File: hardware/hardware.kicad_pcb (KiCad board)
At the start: 2 copper layers, 25.7 x 34.4 mm, 13 parts, among them P1 CONN_01X08, P2 CONN_01X08, P3 CONN_01X02, P4 CONN_01X03

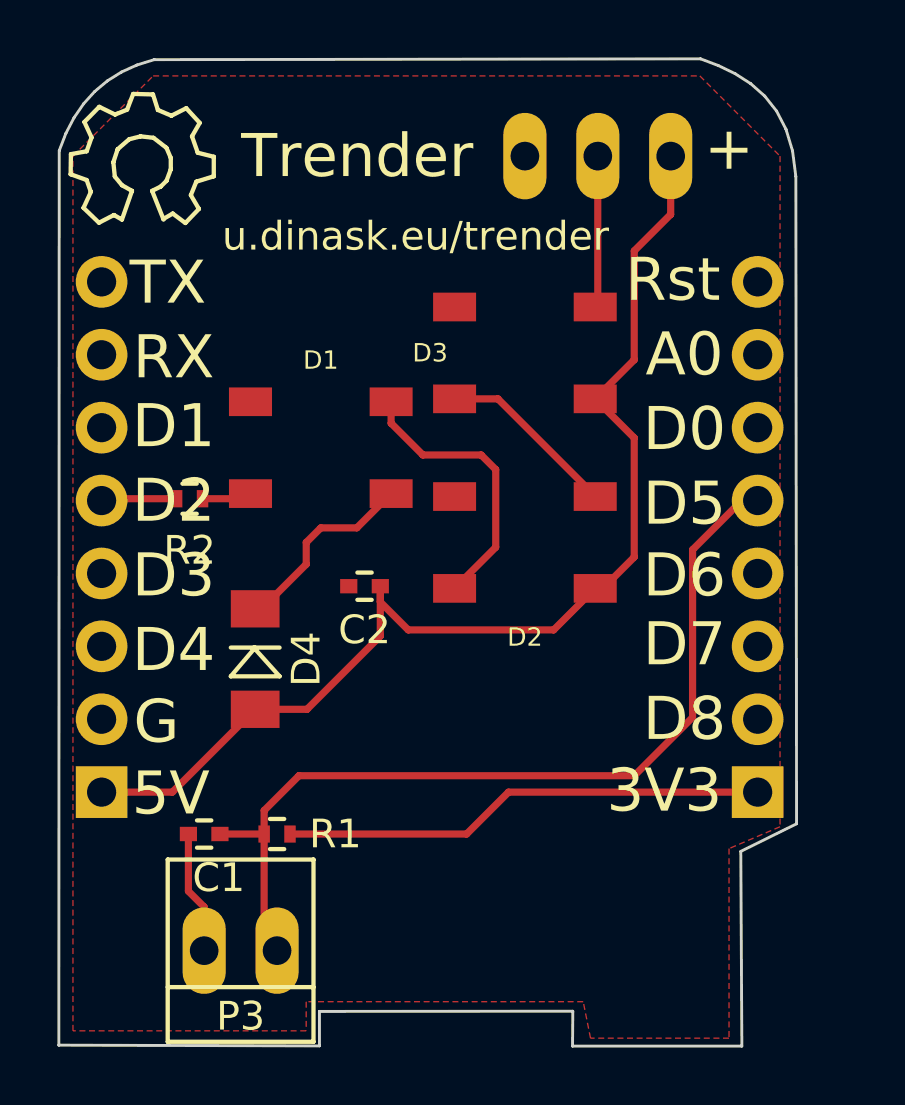
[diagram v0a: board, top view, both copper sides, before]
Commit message: v3.1, refactoring for only one Neopixel
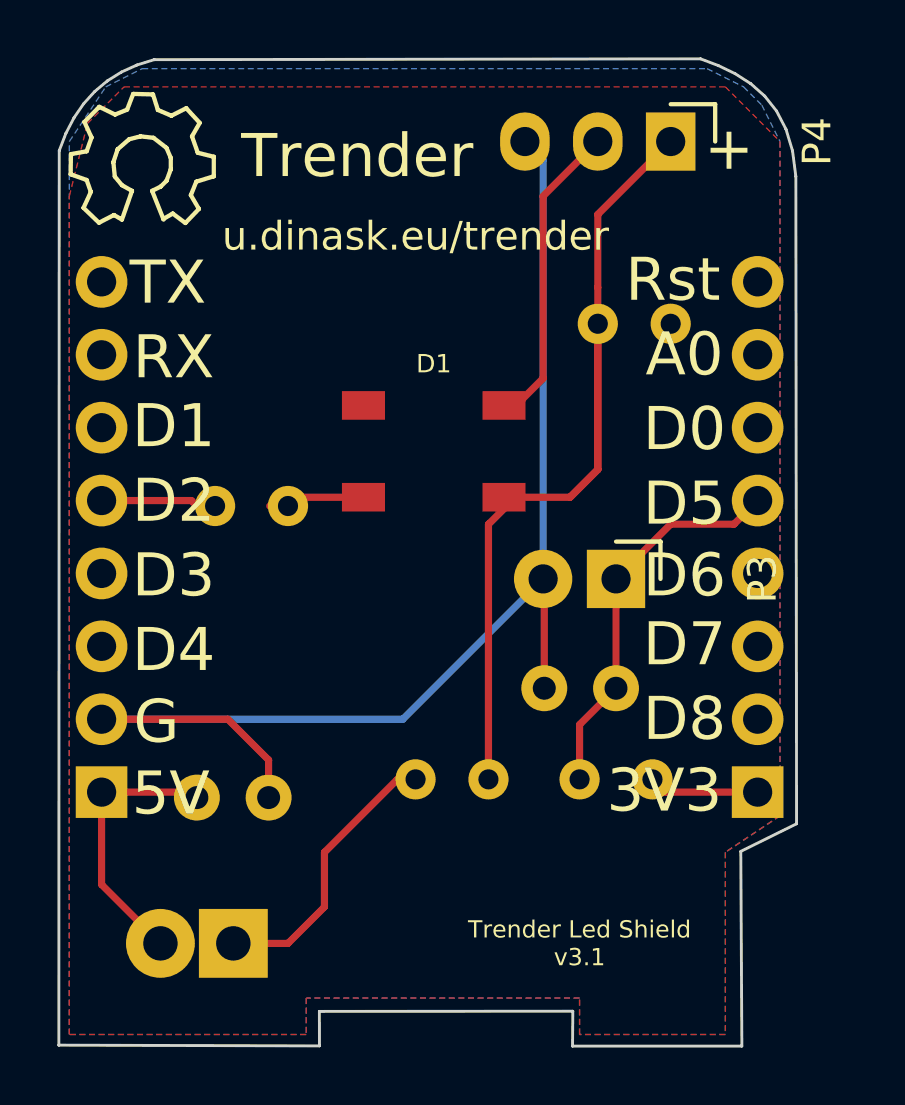
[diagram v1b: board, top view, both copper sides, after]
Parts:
- removed D2, D3: WS2812B, WS2812B:LED_WS2812B
- added R3: R, Resistors_THT:R_Axial_DIN0204_L3.6mm_D1.6mm_P2.54mm_Vertical, B.Cu at (138.4, 103.5)
- added R4: R, Resistors_THT:R_Axial_DIN0204_L3.6mm_D1.6mm_P2.54mm_Vertical, B.Cu at (144.8, 87.6)
- C1, C2: footprint Capacitors_SMD:C_0402 -> Capacitors_THT:C_Disc_D3.8mm_W2.6mm_P2.50mm; moved to B.Cu
- D4: footprint Diodes_SMD:MiniMELF_Standard -> Diodes_THT:D_DO-15_P2.54mm_Vertical_KathodeUp; moved to B.Cu
- P3: footprint Connect:PINHEAD1-2 -> Pin_Headers:Pin_Header_Angled_1x02
- P4: footprint Connect:PINHEAD1-3 -> Pin_Headers:Pin_Header_Angled_1x03; moved to F.Cu
- R1, R2: footprint Resistors_SMD:R_0402 -> Resistors_THT:R_Axial_DIN0204_L3.6mm_D1.6mm_P2.54mm_Vertical; moved to B.Cu
- moved P3 18.4 mm to (145.4, 96.5), turned to 270 degrees
- moved C1 15.2 mm to (145.4, 100.3)
- moved R1 13.2 mm to (146.7, 103.5)
- moved D4 9.94 mm to (132.1, 109.2), turned to 180 degrees
- moved C2 9.40 mm to (130.8, 104.1), turned to 0 degrees
- moved D1 3.94 mm to (139.1, 92.1)
- moved R2 3.44 mm to (134.0, 94.0)
- moved P4 2.59 mm to (147.3, 81.3), turned to 270 degrees
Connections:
- D4 pad 1: Net-(D1-Pad1) -> Net-(D4-Pad1)
- P4 pad 1: /+5V -> Net-(D1-Pad1)
- P4 pad 2: Net-(D3-Pad2) -> Net-(D1-Pad2)
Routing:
- net GND: track 4.75 -> 44.9 mm
- net /+5V: track 41.0 -> 9.52 mm
- net Net-(D1-Pad1): track 6.85 -> 32.6 mm
- net /D5: track 31.7 -> 13.8 mm
- net /+3.3V: track 16.9 -> 5.11 mm
- net Net-(D4-Pad1): track 0.00 -> 10.5 mm
- net Net-(D2-Pad2): track 6.32 -> 0.00 mm
- net Net-(D3-Pad2): track 5.30 -> 0.00 mm
- net Net-(D1-Pad4): track 2.09 -> 3.39 mm
- net Net-(D1-Pad2): track 9.80 -> 10.8 mm
- net /D2: track 2.64 -> 3.49 mm
- added copper zone on B.Cu, net GND
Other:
- board text added: "Trender Led Shield v3.1"
